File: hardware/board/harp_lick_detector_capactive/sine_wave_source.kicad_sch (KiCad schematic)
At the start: 8 parts

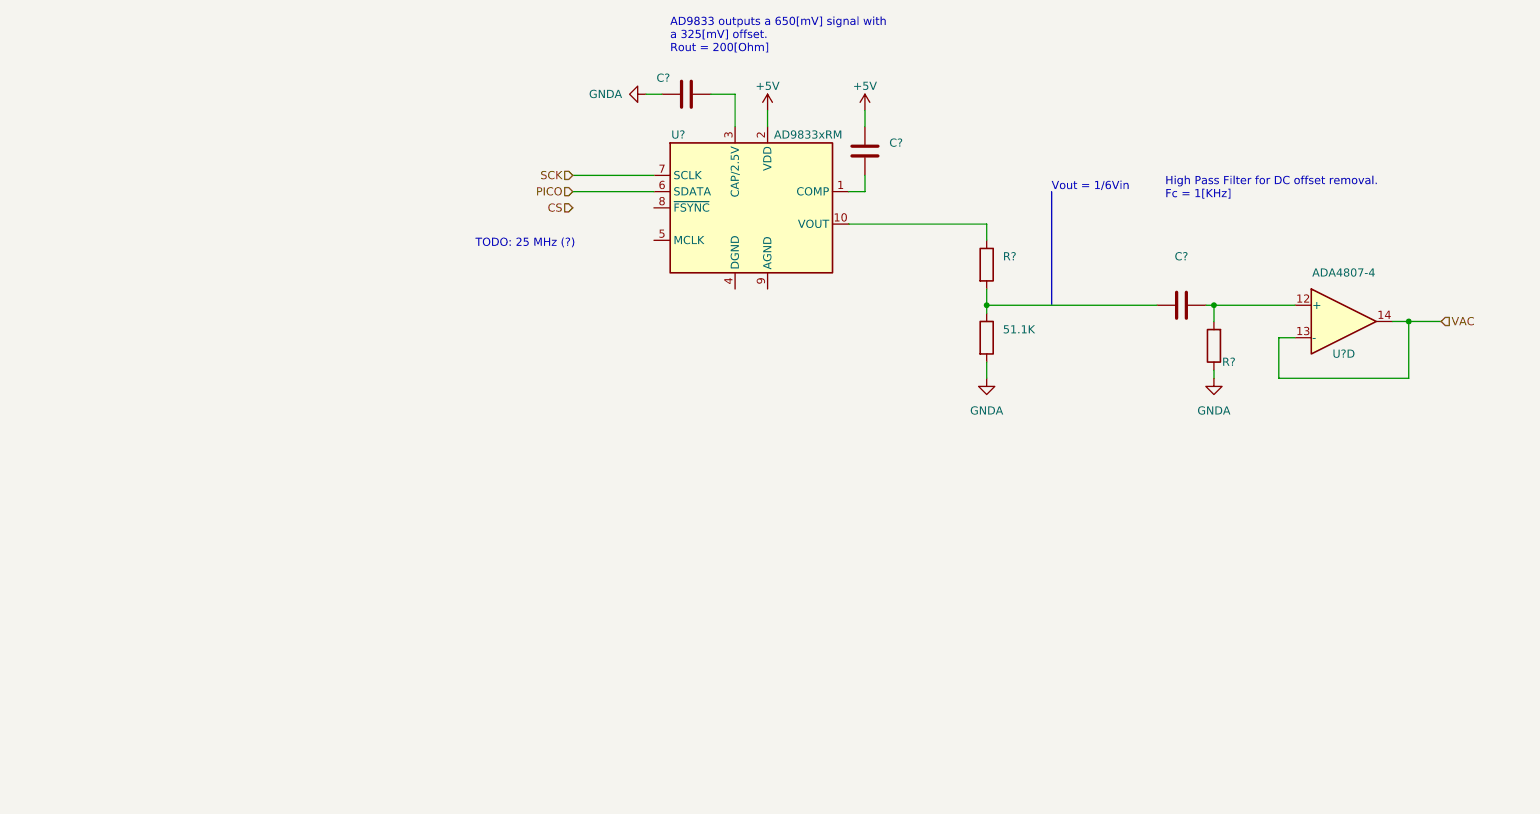
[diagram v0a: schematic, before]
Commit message: add pico-sdk; draft as9833 driver
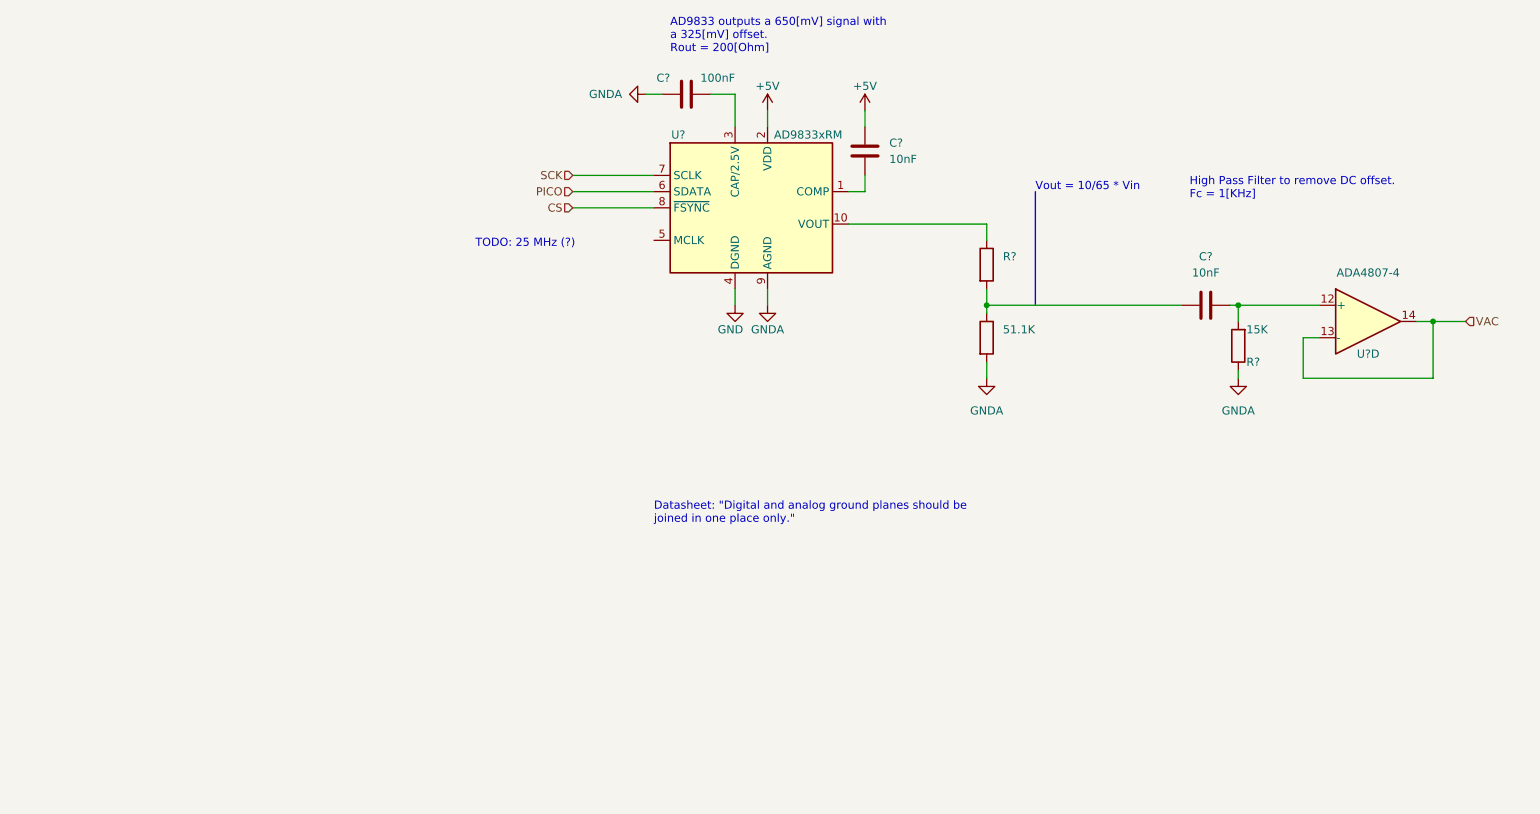
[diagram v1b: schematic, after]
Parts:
- C?: value (none) -> 100nF
- C? (x2): value (none) -> 10nF
- R?: value (none) -> 15K
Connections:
- net CS: now also U?.8 (~{FSYNC})
- net GNDA: now also U?.9 (AGND)
- net GND: now reaches U?.4 (DGND)
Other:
- note added: "Datasheet: "Digital and analog ground planes should be joined in one place only.""
- note added: "High Pass Filter to remove DC offset. Fc = 1[KHz]"
- note added: "Vout = 10/65 * Vin"
- note removed: "High Pass Filter for DC offset removal. Fc = 1[KHz]"
- note removed: "Vout = 1/6Vin"
- moved on the sheet: C?, R?, U?D

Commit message: update schematic
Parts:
- R?: value (none) -> 10K
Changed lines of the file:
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@@
       (effects (font (size 1.27 1.27)) (justify left))
     )
-    (property "Value" "" (id 1) (at 175.26 102.8699 0)
+    (property "Value" "10K" (id 1) (at 175.26 102.8699 0)
       (effects (font (size 1.27 1.27)) (justify left))
     )

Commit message: draft wheatstone implementation
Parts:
- renumbered 51.1K to 51.1K?
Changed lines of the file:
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@@
   (symbol (lib_id "Device:R") (at 172.72 113.03 0) (unit 1)
     (in_bom yes) (on_board yes) (fields_autoplaced)
-    (property "Reference" "51.1K" (id 0) (at 175.26 111.7599 0)
+    (property "Reference" "51.1K?" (id 0) (at 175.26 111.7599 0)
       (effects (font (size 1.27 1.27)) (justify left))
     )

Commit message: update analog front end
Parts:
- removed U?: ADA4807-4, symbol Amplifier_Operational:ADA4807-4
- added U?: (no value), symbol Amplifier_Operational:ADA4807-1
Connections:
- net at C?.2, R?.2: now also U?.3 (+)
- new net VSIN: U?.1, U?.4 (-)
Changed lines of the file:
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@@
     (effects (font (size 1.27 1.27)) (justify left bottom))
   )
-  (hierarchical_label "VAC" (shape input) (at 247.65 110.49 0)
+  (hierarchical_label "VSIN" (shape input) (at 247.65 110.49 0)
     (effects (font (size 1.27 1.27)) (justify left))
   )
@@
     (pin "2")
   )
-  (symbol (lib_id "Amplifier_Operational:ADA4807-4") (at 232.41 110.49 0) (unit 4)
-    (in_bom yes) (on_board yes)
-    (property "Reference" "U?" (id 0) (at 232.41 115.57 0))
-    (property "Value" "ADA4807-4" (id 1) (at 232.41 102.87 0))
-    (property "Footprint" "" (id 2) (at 231.14 107.95 0)
-      (effects (font (size 1.27 1.27)) hide)
-    )
-    (property "Datasheet" "https://www.analog.com/media/en/technical-documentation/data-sheets/ADA4807-1_4807-2_4807-4.pdf" (id 3) (at 233.68 105.41 0)
-      (effects (font (size 1.27 1.27)) hide)
-    )
-    (pin "1")
-    (pin "2")
-    (pin "3")
-    (pin "5")
-    (pin "6")
-    (pin "7")
-    (pin "10")
-    (pin "8")
-    (pin "9")
-    (pin "12")
-    (pin "13")
-    (pin "14")
-    (pin "11")
-    (pin "4")
-  )
   (symbol (lib_id "power:+5V") (at 138.43 77.47 0) (unit 1)
     (in_bom yes) (on_board yes)
@@
     (pin "2")
   )
+  (symbol (lib_id "Amplifier_Operational:ADA4807-1") (at 232.41 110.49 0) (unit 1)
+    (in_bom yes) (on_board yes) (fields_autoplaced)
+    (property "Reference" "U?" (id 0) (at 245.11 105.791 0))
+    (property "Value" "" (id 1) (at 245.11 108.331 0))
+    (property "Footprint" "" (id 2) (at 232.41 116.84 0)
+      (effects (font (size 1.27 1.27)) hide)
+    )
+    (property "Datasheet" "https://www.analog.com/media/en/technical-documentation/data-sheets/ADA4807-1_4807-2_4807-4.pdf" (id 3) (at 232.41 119.38 0)
+      (effects (font (size 1.27 1.27)) (justify left) hide)
+    )
+    (pin "1")
+    (pin "2")
+    (pin "3")
+    (pin "4")
+    (pin "5")
+    (pin "6")
+  )
   (symbol (lib_id "power:GNDA") (at 212.09 119.38 0) (unit 1)

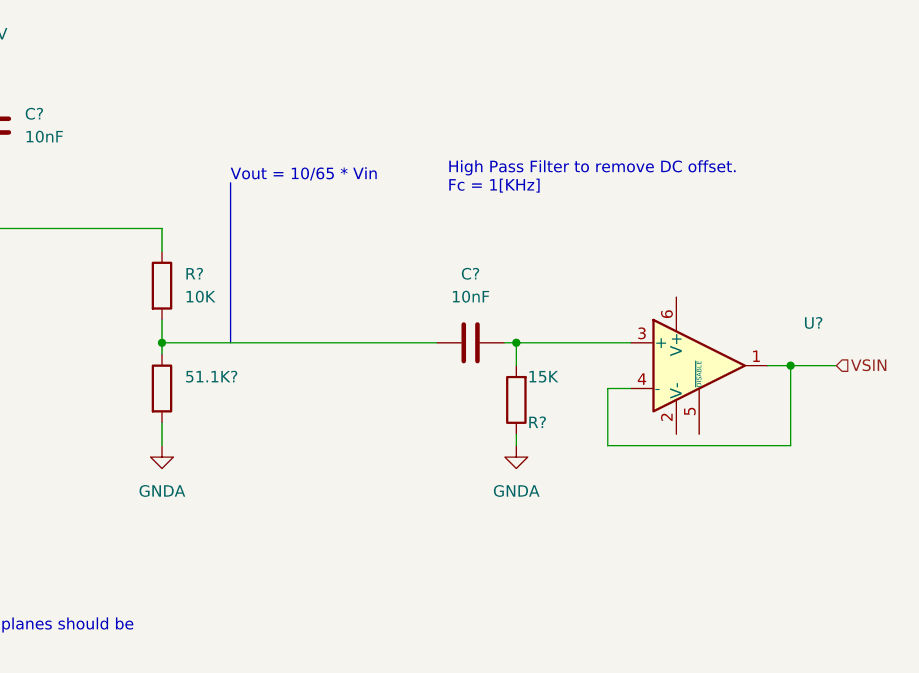
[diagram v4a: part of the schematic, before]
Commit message: update sine wave generator
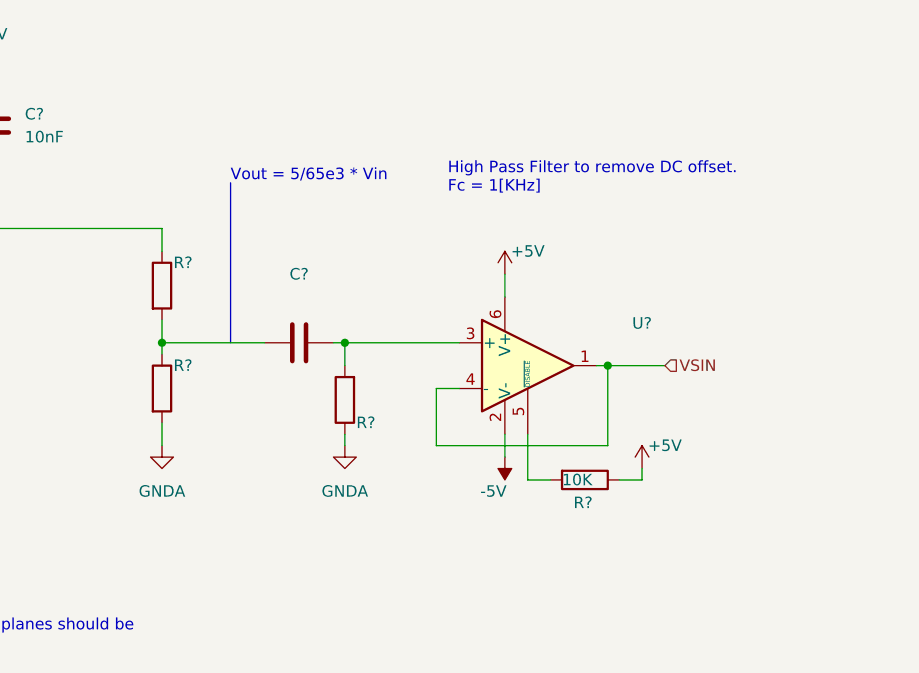
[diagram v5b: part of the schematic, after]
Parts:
- removed 51.1K?: ~, symbol Device:R
- added R?: (no value), symbol Device:R
- added R?: 10K, Resistor_SMD:R_0402_1005Metric_Pad0.72x0.64mm_HandSolder, symbol Device:R
- C?: value 10nF -> (none)
- R?: value 15K -> (none)
- R?: value 10K -> (none)
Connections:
- net +5V: now also U?.6 (V+), R?.1
- net GNDA: now also R?.2
- net at U?.10 (VOUT): now also R?.1; no longer R?.1
- net at C?.1: now also R?.1, R?.2; no longer R?.2
- net -5V: now reaches U?.2 (V-)
- net at U?.5 (~{DISABLE}): now also R?.2
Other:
- note added: "Vout = 5/65e3 * Vin"
- note removed: "Vout = 10/65 * Vin"
- moved on the sheet: C?, R?, U?

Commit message: assign sch components partial
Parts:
- removed R?: 10K, Resistor_SMD:R_0402_1005Metric_Pad0.72x0.64mm_HandSolder, symbol Device:R
- removed U?: (no value), symbol Amplifier_Operational:ADA4807-1
- added C? (x3): (no value), symbol Device:C
- added U3: (no value), symbol Amplifier_Operational:ADA4807-2ARM
- added X1: (no value), symbol Oscillator:ASE-xxxMHz
- C?: value 100nF -> (none)
- C?: value 10nF -> (none)
- U4: renamed from U?; value AD9833xRM -> (none); footprint Package_SO:MSOP-10_3x3mm_P0.5mm -> (none)
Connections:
- net +5V: now also U3.8 (V+); no longer C?.2, U4.2 (VDD)
- net -5V: now also U3.4 (V-)
- net GNDA: now also C?.1, C?.1, C?.1, X1.2 (GND)
- net VSIN: now also U3.1, U3.2 (-)
- net at U4.5 (MCLK): now also X1.3 (OUT)
- net at R?.1, R?.2: now also U3.5 (+); no longer C?.1
- net at C?.2, R?.2: now also U3.3 (+)
- new net: C?.1, U3.6 (-), U3.7
- new net +3V3: C?.2, C?.2, C?.2, C?.2, U4.2 (VDD), X1.4 (Vdd)
- no-connect marks 0 -> 1
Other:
- note added: "Function Generator Bypass Caps"
- note added: "Oscillator Bypass Cap"
- note removed: "TODO: 25 MHz (?)"
- moved on the sheet: C?, R?

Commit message: assign more sch components
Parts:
- C?: Link (none) -> https://www.digikey.com/en/products/detail/murata-electroni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; Manufacturer (none) -> Murata Electronics; Manufacturer Number (none) -> GRM21BZ71E106KE15L; Rated Voltage (none) -> 25V; Temperature Coefficient (none) -> X7R
- C? (x2): Link (none) -> https://www.digikey.com/en/products/detail/samsung-electro-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; Manufacturer (none) -> Samsung Electro-Mechanics; Manufacturer Number (none) -> CL10B104KB8NNWC; Rated Voltage (none) -> 50V; Temperature Coefficient (none) -> X7R; Tolerance (none) -> 10%
- C? (x2): Link (none) -> https://www.digikey.com/en/products/detail/kemet/C0603X103J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; Manufacturer (none) -> Kemet; Manufacturer Number (none) -> C0603X103J5RECAUTO; Rated Voltage (none) -> 50V; Temperature Coefficient (none) -> X7R; Tolerance (none) -> 5%
- C?: Link (none) -> https://www.digikey.com/en/products/detail/kemet/C0603C102J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; Manufacturer (none) -> Kemet; Manufacturer Number (none) -> C0603C102J5RAC7411; Rated Voltage (none) -> 50V; Temperature Coefficient (none) -> X7R; Tolerance (none) -> 5%
- R?: Link (none) -> https://www.digikey.com/en/products/detail/te-connectivity-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; Manufacturer (none) -> TE Connectivity Passive Product; Manufacturer Number (none) -> CRGP0603F150K; Tolerance (none) -> 1%
- U3: Link (none) -> https://www.digikey.com/en/products/detail/analog-devices-i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; Manufacturer (none) -> Analog Devices Inc.; Manufacturer Number (none) -> ADA4807-2ARMZ
- U4: Link (none) -> https://www.digikey.com/en/products/detail/analog-devices-i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; Manufacturer (none) -> Analog Devices Inc.; Manufacturer Number (none) -> AD9833BRMZ-REEL7

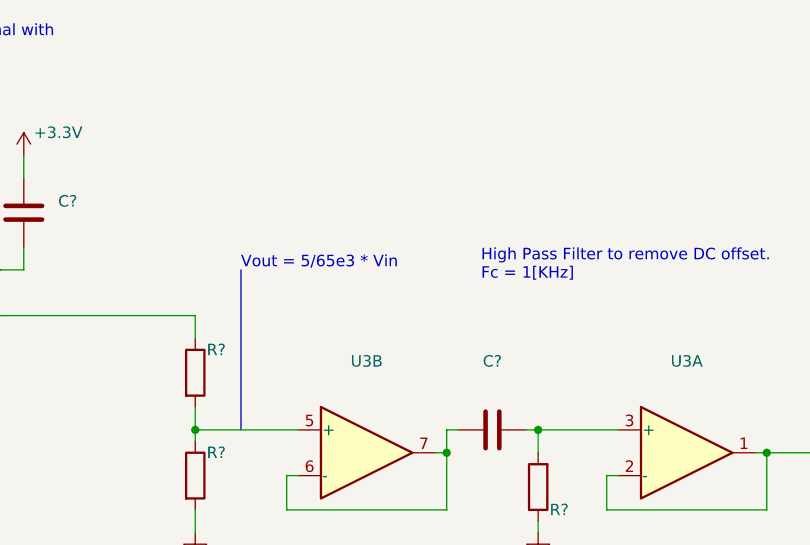
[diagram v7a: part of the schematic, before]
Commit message: assign more components
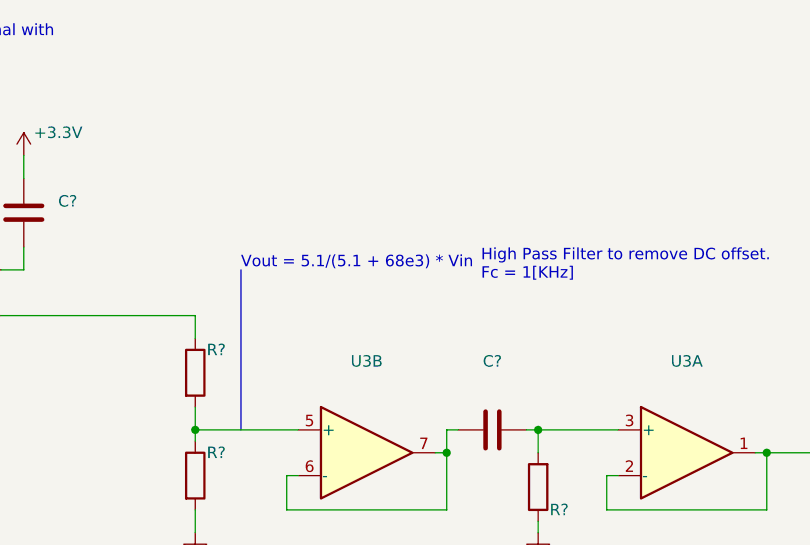
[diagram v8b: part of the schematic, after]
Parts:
- R?: Link (none) -> https://www.digikey.com/en/products/detail/te-connectivity-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; Manufacturer (none) -> TE Connectivity Passive Product; Manufacturer Number (none) -> CRGP0603F68K; Tolerance (none) -> 1%
- R?: Link (none) -> https://www.digikey.com/en/products/detail/panasonic-electr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; Manufacturer (none) -> Panasonic Electronic Components; Manufacturer Number (none) -> ERJ-3BQF5R1V; Tolerance (none) -> 1%
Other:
- note added: "Vout = 5.1/(5.1 + 68e3) * Vin"
- note removed: "Vout = 5/65e3 * Vin"
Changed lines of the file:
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@@
     (effects (font (size 1.27 1.27)) (justify left bottom))
   )
-  (text "Vout = 5/65e3 * Vin" (at 177.8 90.17 0)
+  (text "Vout = 5.1/(5.1 + 68e3) * Vin" (at 177.8 90.17 0)
     (effects (font (size 1.27 1.27)) (justify left bottom))
   )
@@
       (effects (font (size 1.27 1.27)) hide)
     )
-    (property "Datasheet" "~" (id 3) (at 172.72 101.6 0)
+    (property "Datasheet" "https://www.te.com/usa-en/product-4-2176326-7.datasheet.pdf" (id 3) (at 172.72 101.6 0)
+      (effects (font (size 1.27 1.27)) hide)
+    )
+    (property "Link" "https://www.digikey.com/en/products/detail/te-connectivity-passive-product/CRGP0603F68K/8577040" (id 4) (at 172.72 101.6 0)
+      (effects (font (size 1.27 1.27)) hide)
+    )
+    (property "Manufacturer" "TE Connectivity Passive Product" (id 5) (at 172.72 101.6 0)
+      (effects (font (size 1.27 1.27)) hide)
+    )
+    (property "Manufacturer Number" "CRGP0603F68K" (id 6) (at 172.72 101.6 0)
+      (effects (font (size 1.27 1.27)) hide)
+    )
+    (property "Tolerance" "1%" (id 7) (at 172.72 101.6 0)
       (effects (font (size 1.27 1.27)) hide)
     )
@@
       (effects (font (size 1.27 1.27)) hide)
     )
-    (property "Datasheet" "~" (id 3) (at 172.72 113.03 0)
-      (effects (font (size 1.27 1.27)) hide)
-    )
+    (property "Datasheet" "https://industrial.panasonic.com/cdbs/www-data/pdf/RDN0000/AOA0000C313.pdf" (id 3) (at 172.72 113.03 0)
+      (effects (font (size 1.27 1.27)) hide)
+    )
+    (property "Link" "https://www.digikey.com/en/products/detail/panasonic-electronic-components/ERJ-3BQF5R1V/5647419" (id 4) (at 172.72 113.03 0)
+      (effects (font (size 1.27 1.27)) hide)
+    )
+    (property "Manufacturer" "Panasonic Electronic Components" (id 5) (at 172.72 113.03 0)
+      (effects (font (size 1.27 1.27)) hide)
+    )
+    (property "Manufacturer Number" "ERJ-3BQF5R1V" (id 6) (at 172.72 113.03 0)
+      (effects (font (size 1.27 1.27)) hide)
+    )
+    (property "Tolerance" "1%" (id 7) (at 172.72 113.03 0)
+      (effects (font (size 1.27 1.27)) hide)
+    )
